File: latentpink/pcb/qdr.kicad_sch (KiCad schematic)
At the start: 69 parts, among them U2 XC7K160T-2FBG484C, U28 IS25WP256D-JLLE, U29 DSC1123CI2-150.0000T, U3 CY7C2245KV18-450BZXI

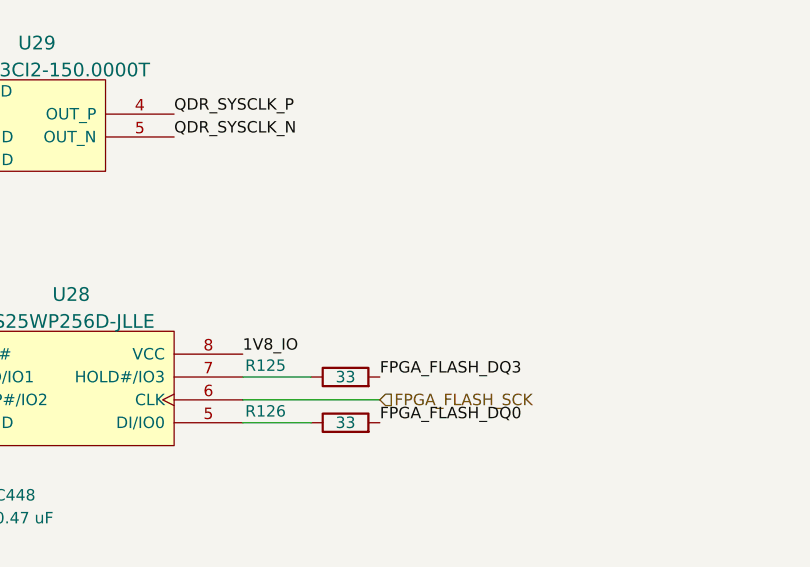
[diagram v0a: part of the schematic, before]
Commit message: Added some debug LEDs, PMOD, and temp sensors
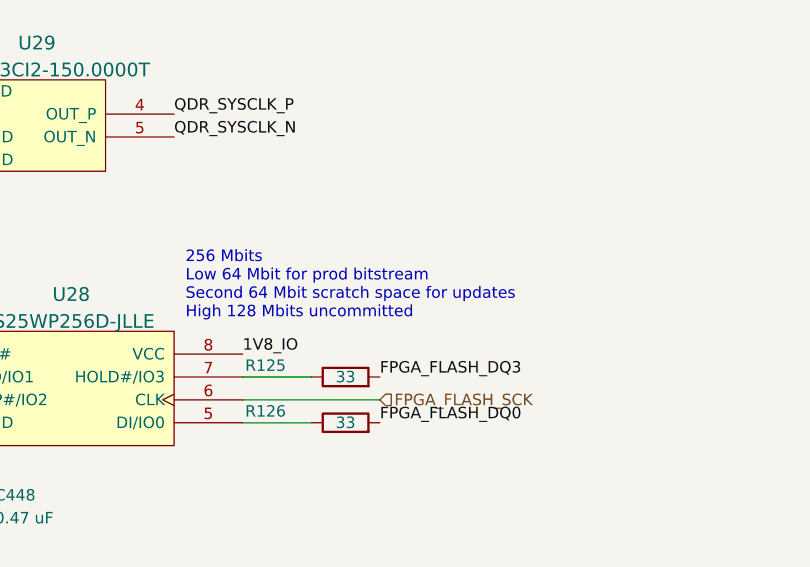
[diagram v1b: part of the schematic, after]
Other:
- note added: "256 Mbits Low 64 Mbit for prod bitstream Second 64 Mbit scratch space for updates High 128 Mbits uncommitted"
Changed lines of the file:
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@@
+    (effects (font (size 1.27 1.27)) (justify left bottom))
+  )
+  (text "256 Mbits\nLow 64 Mbit for prod bitstream\nSecond 64 Mbit scratch space for updates\nHigh 128 Mbits uncommitted"
+    (at 285.75 236.22 0)
     (effects (font (size 1.27 1.27)) (justify left bottom))
   )

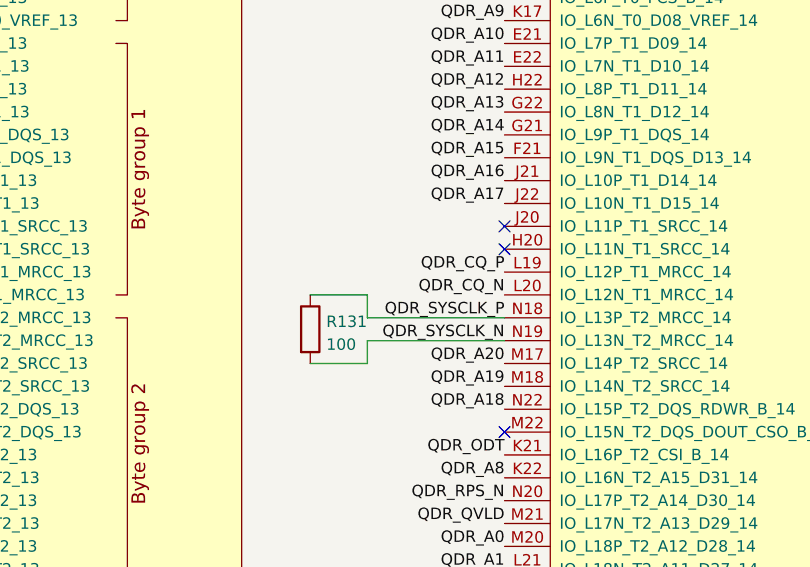
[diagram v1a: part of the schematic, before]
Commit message: Continued work on signoff review, added some more test points and SFP+ activity LEDs
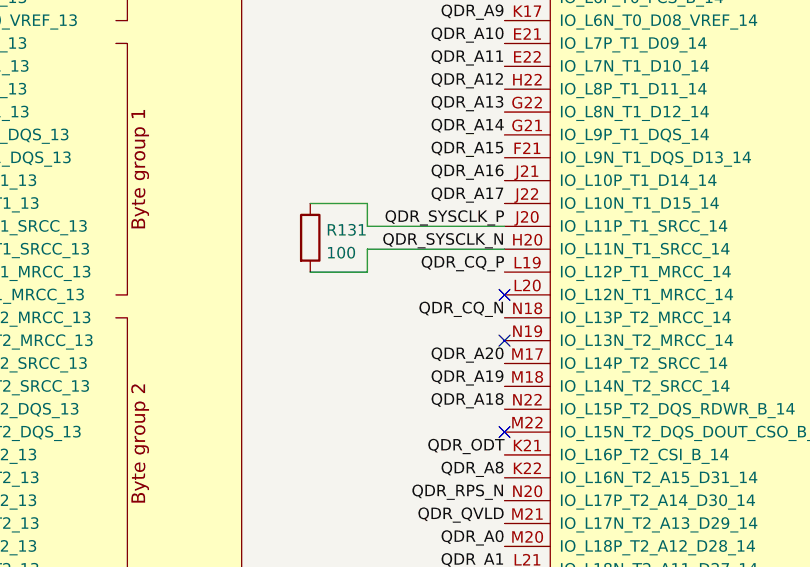
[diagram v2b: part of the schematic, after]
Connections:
- net QDR_CQ_N: now also U2.N18 (IO_L13P_T2_MRCC_14); no longer U2.L20 (IO_L12N_T1_MRCC_14)
- net QDR_SYSCLK_N: now also U2.H20 (IO_L11N_T1_SRCC_14); no longer U2.N19 (IO_L13N_T2_MRCC_14)
- net QDR_SYSCLK_P: now also U2.J20 (IO_L11P_T1_SRCC_14); no longer U2.N18 (IO_L13P_T2_MRCC_14)
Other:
- moved on the sheet: R131
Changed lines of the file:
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@@
   (paper "A3")
   (title_block
-    (date "2023-05-20")
+    (date "2023-05-21")
     (rev "0.1")
     (company "Antikernel Labs")
@@
   (no_connect (at 198.12 25.4))
   (no_connect (at 346.71 132.08))
-  (no_connect (at 269.24 78.74))
   (no_connect (at 346.71 99.06))
   (no_connect (at 33.02 181.61))
@@
   (no_connect (at 346.71 25.4))
   (no_connect (at 346.71 40.64))
-  (no_connect (at 269.24 81.28))
   (no_connect (at 346.71 38.1))
   (no_connect (at 269.24 149.86))
@@
   (no_connect (at 269.24 147.32))
   (no_connect (at 33.02 179.07))
+  (no_connect (at 269.24 91.44))
   (no_connect (at 346.71 71.12))
   (no_connect (at 269.24 139.7))
@@
   (no_connect (at 346.71 86.36))
   (no_connect (at 200.66 266.7))
+  (no_connect (at 269.24 86.36))
   (wire (pts (xy 88.9 209.55) (xy 101.6 209.55))
     (stroke (width 0) (type default) (color 0 0 0 0))
@@
     (stroke (width 0) (type default) (color 0 0 0 0))
   )
-  (wire (pts (xy 254 93.98) (xy 247.65 93.98))
+  (wire (pts (xy 254 83.82) (xy 247.65 83.82))
     (stroke (width 0) (type default) (color 0 0 0 0))
   )
@@
     (stroke (width 0) (type default) (color 0 0 0 0))
   )
-  (wire (pts (xy 254 88.9) (xy 254 86.36))
+  (wire (pts (xy 254 78.74) (xy 254 76.2))
     (stroke (width 0) (type default) (color 0 0 0 0))
   )
@@
     (stroke (width 0) (type default) (color 0 0 0 0))
   )
-  (wire (pts (xy 254 86.36) (xy 247.65 86.36))
+  (wire (pts (xy 254 76.2) (xy 247.65 76.2))
     (stroke (width 0) (type default) (color 0 0 0 0))
   )
@@
     (stroke (width 0) (type default) (color 0 0 0 0))
   )
-  (wire (pts (xy 254 91.44) (xy 254 93.98))
+  (wire (pts (xy 254 81.28) (xy 254 83.82))
     (stroke (width 0) (type default) (color 0 0 0 0))
   )
@@
     (stroke (width 0) (type default) (color 0 0 0 0))
   )
-  (wire (pts (xy 269.24 88.9) (xy 254 88.9))
+  (wire (pts (xy 269.24 78.74) (xy 254 78.74))
     (stroke (width 0) (type default) (color 0 0 0 0))
   )
@@
     (stroke (width 0) (type default) (color 0 0 0 0))
   )
-  (wire (pts (xy 269.24 91.44) (xy 254 91.44))
+  (wire (pts (xy 269.24 81.28) (xy 254 81.28))
     (stroke (width 0) (type default) (color 0 0 0 0))
   )
@@
     (effects (font (size 1.27 1.27)) (justify right bottom))
   )
-  (label "QDR_SYSCLK_N" (at 269.24 91.44 180)
+  (label "QDR_SYSCLK_N" (at 269.24 81.28 180)
     (effects (font (size 1.27 1.27)) (justify right bottom))
   )
@@
     (effects (font (size 1.27 1.27)) (justify right bottom))
   )
-  (label "QDR_SYSCLK_P" (at 269.24 88.9 180)
+  (label "QDR_SYSCLK_P" (at 269.24 78.74 180)
     (effects (font (size 1.27 1.27)) (justify right bottom))
   )
@@
     (effects (font (size 1.27 1.27)) (justify right bottom))
   )
-  (label "QDR_CQ_N" (at 269.24 86.36 180)
+  (label "QDR_CQ_N" (at 269.24 88.9 180)
     (effects (font (size 1.27 1.27)) (justify right bottom))
   )
@@
     (pin "2")
   )
-  (symbol (lib_id "device:R") (at 247.65 90.17 0) (unit 1)
+  (symbol (lib_id "device:R") (at 247.65 80.01 0) (unit 1)
     (in_bom yes) (on_board yes) (fields_autoplaced)
-    (property "Reference" "R131" (id 0) (at 249.428 89.3353 0)
+    (property "Reference" "R131" (id 0) (at 249.428 79.1753 0)
       (effects (font (size 1.27 1.27)) (justify left))
     )
-    (property "Value" "100" (id 1) (at 249.428 91.8722 0)
+    (property "Value" "100" (id 1) (at 249.428 81.7122 0)
       (effects (font (size 1.27 1.27)) (justify left))
     )
-    (property "Footprint" "azonenberg_pcb:EIA_0402_RES_NOSILK" (id 2) (at 245.872 90.17 90)
+    (property "Footprint" "azonenberg_pcb:EIA_0402_RES_NOSILK" (id 2) (at 245.872 80.01 90)
       (effects (font (size 1.27 1.27)) hide)
     )
-    (property "Datasheet" "" (id 3) (at 247.65 90.17 0)
+    (property "Datasheet" "" (id 3) (at 247.65 80.01 0)
       (effects (font (size 1.27 1.27)) hide)
     )

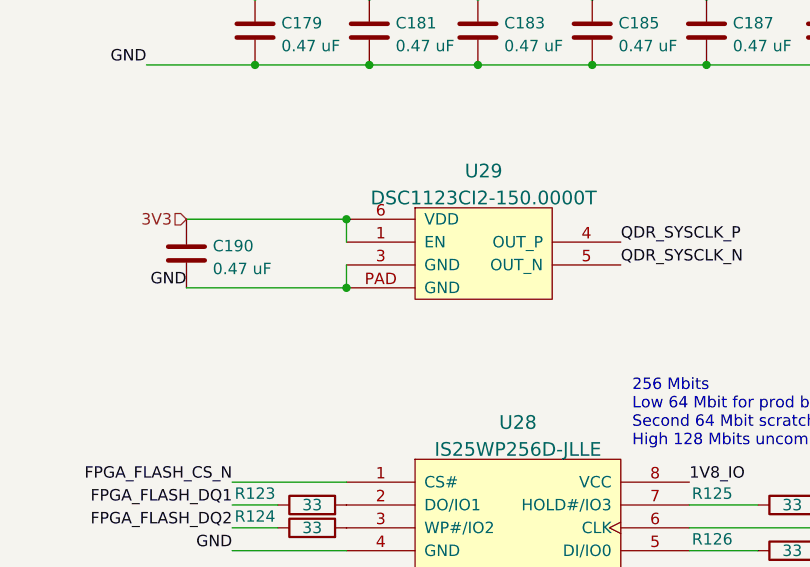
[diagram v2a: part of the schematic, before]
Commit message: Preliminary routing of first four baseT interfaces on VSC8512
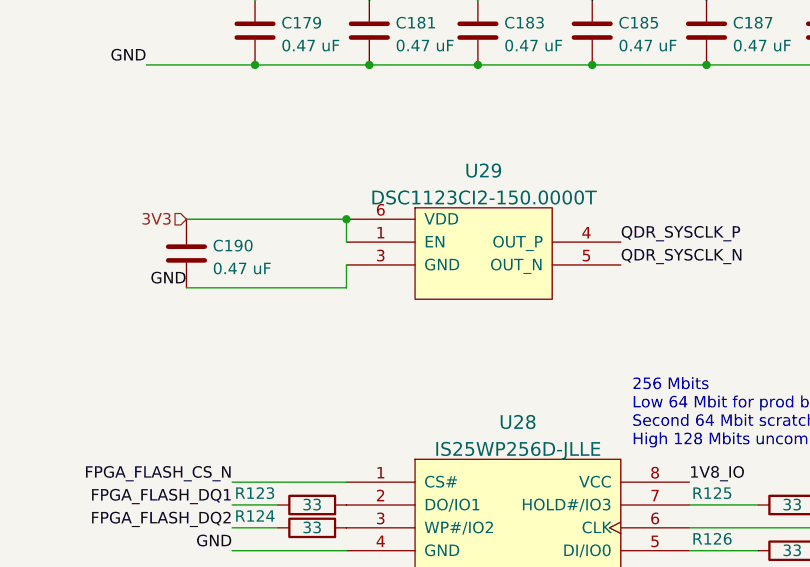
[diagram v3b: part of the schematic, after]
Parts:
- U29: symbol osc-azonenberg:OSC_LVDS -> osc-azonenberg:OSC_LVDS_NOPAD
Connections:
- net GND: no longer U29.PAD (GND)
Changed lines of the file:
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@@
   (junction (at 143.51 217.17) (diameter 0) (color 0 0 0 0)
   )
-  (junction (at 254 218.44) (diameter 0) (color 0 0 0 0)
-  )
   (junction (at 62.23 201.93) (diameter 0) (color 0 0 0 0)
   )
@@
     (pin "2")
   )
-  (symbol (lib_id "osc-azonenberg:OSC_LVDS") (at 261.62 219.71 0) (unit 1)
+  (symbol (lib_id "osc-azonenberg:OSC_LVDS_NOPAD") (at 261.62 219.71 0) (unit 1)
     (in_bom yes) (on_board yes) (fields_autoplaced)
     (property "Reference" "U29" (id 0) (at 269.24 205.4659 0)
@@
     (pin "5")
     (pin "6")
-    (pin "PAD")
   )
   (symbol (lib_id "device:R_Pack04") (at 205.74 227.33 90) (unit 1)

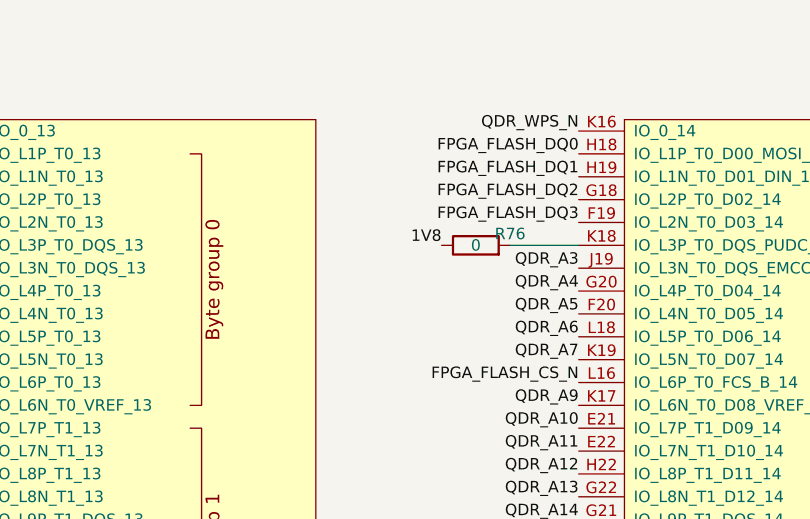
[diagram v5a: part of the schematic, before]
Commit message: Rearranged all unplaced components and grouped by functional subsystem
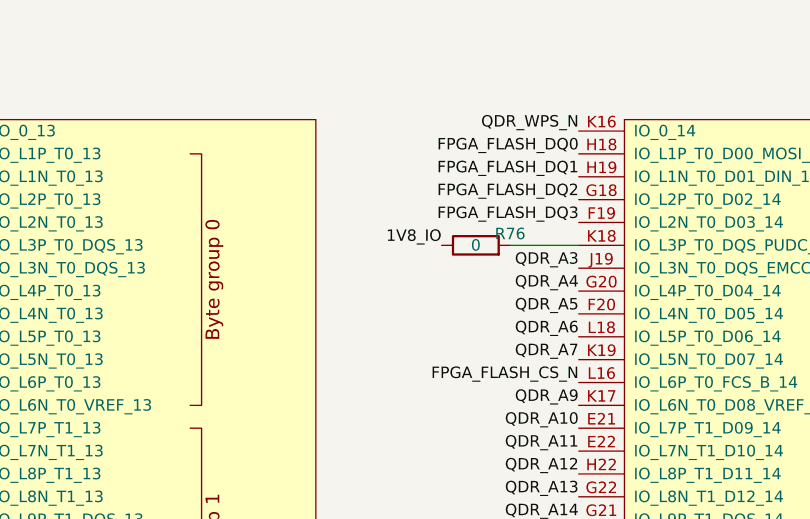
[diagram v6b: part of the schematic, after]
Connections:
- net 1V8: no longer R76.1
- net 1V8_IO: now also R76.1
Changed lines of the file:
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@@
     (effects (font (size 1.27 1.27)) (justify right bottom))
   )
-  (label "1V8" (at 254 38.1 180)
+  (label "1V8_IO" (at 254 38.1 180)
     (effects (font (size 1.27 1.27)) (justify right bottom))
   )
@@
   )
   (symbol (lib_id "device:C") (at 243.84 178.435 0) (unit 1)
-    (in_bom yes) (on_board yes) (fields_autoplaced)
+    (in_bom yes) (on_board yes)
     (property "Reference" "C178" (id 0) (at 246.761 177.6003 0)
       (effects (font (size 1.27 1.27)) (justify left))
